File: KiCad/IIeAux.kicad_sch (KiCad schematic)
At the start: 15 parts, among them J1 Aux Slot, U1 SN74LVC245AN, U2 TangNano9K, U3 74LS245, U4 74LS374, U5 SN74LVC245AN, U6 SN74LVC245AN

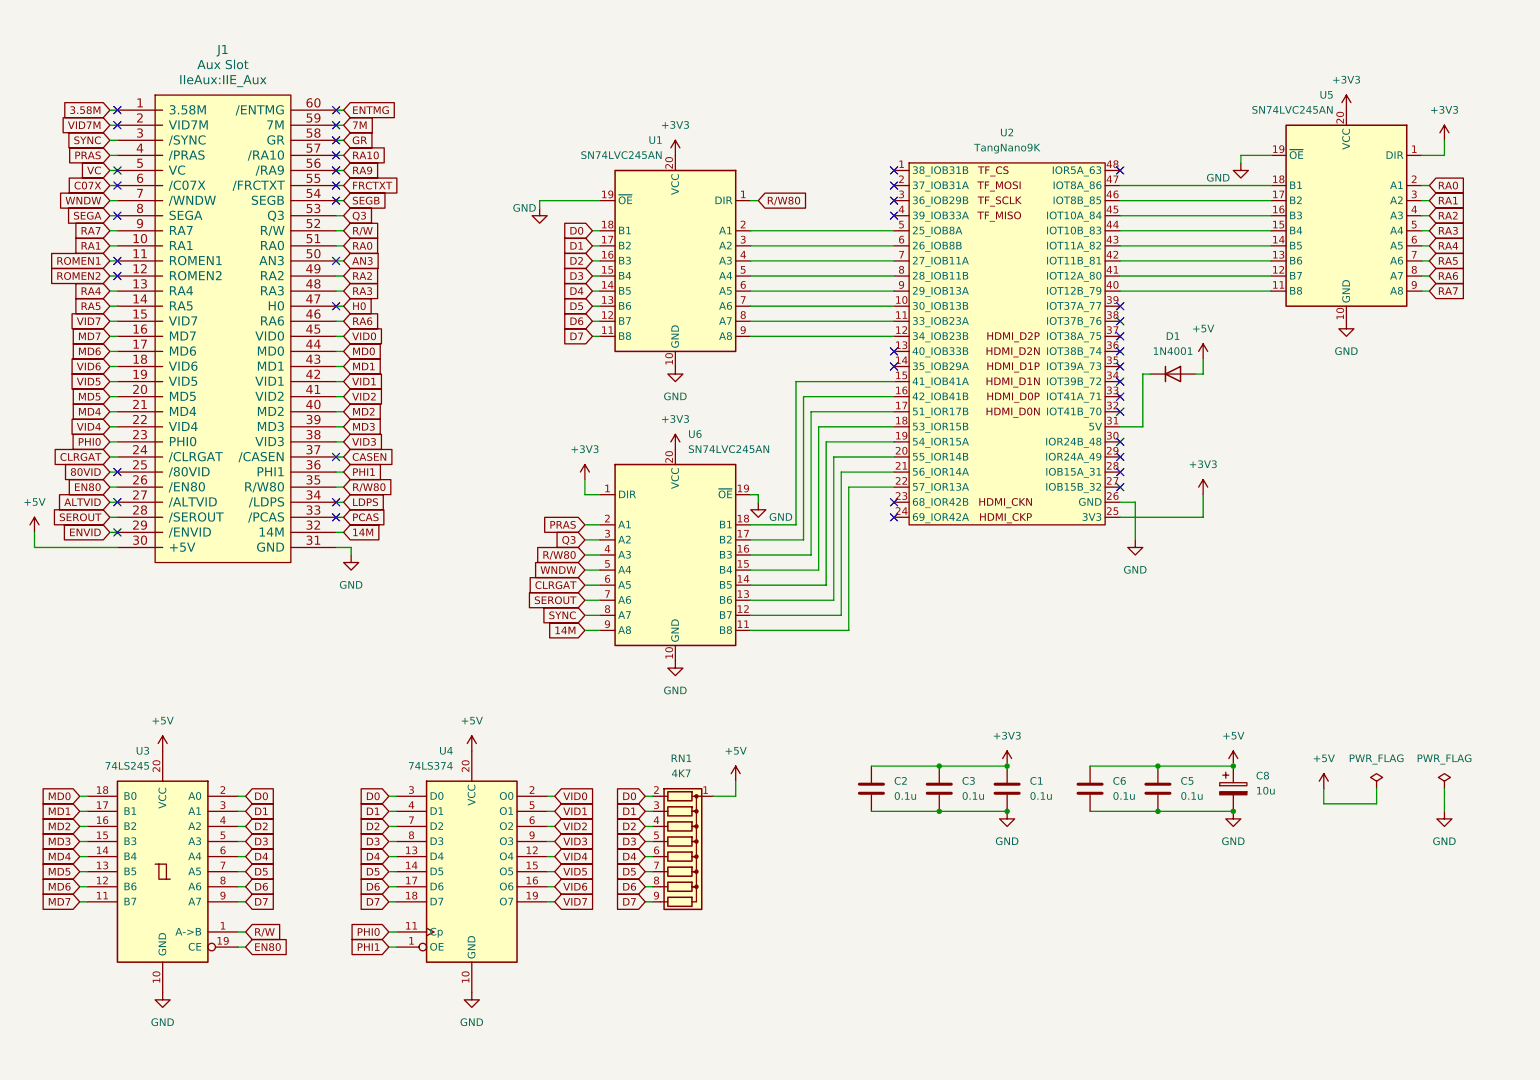
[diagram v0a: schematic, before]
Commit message: extended 64K RAM
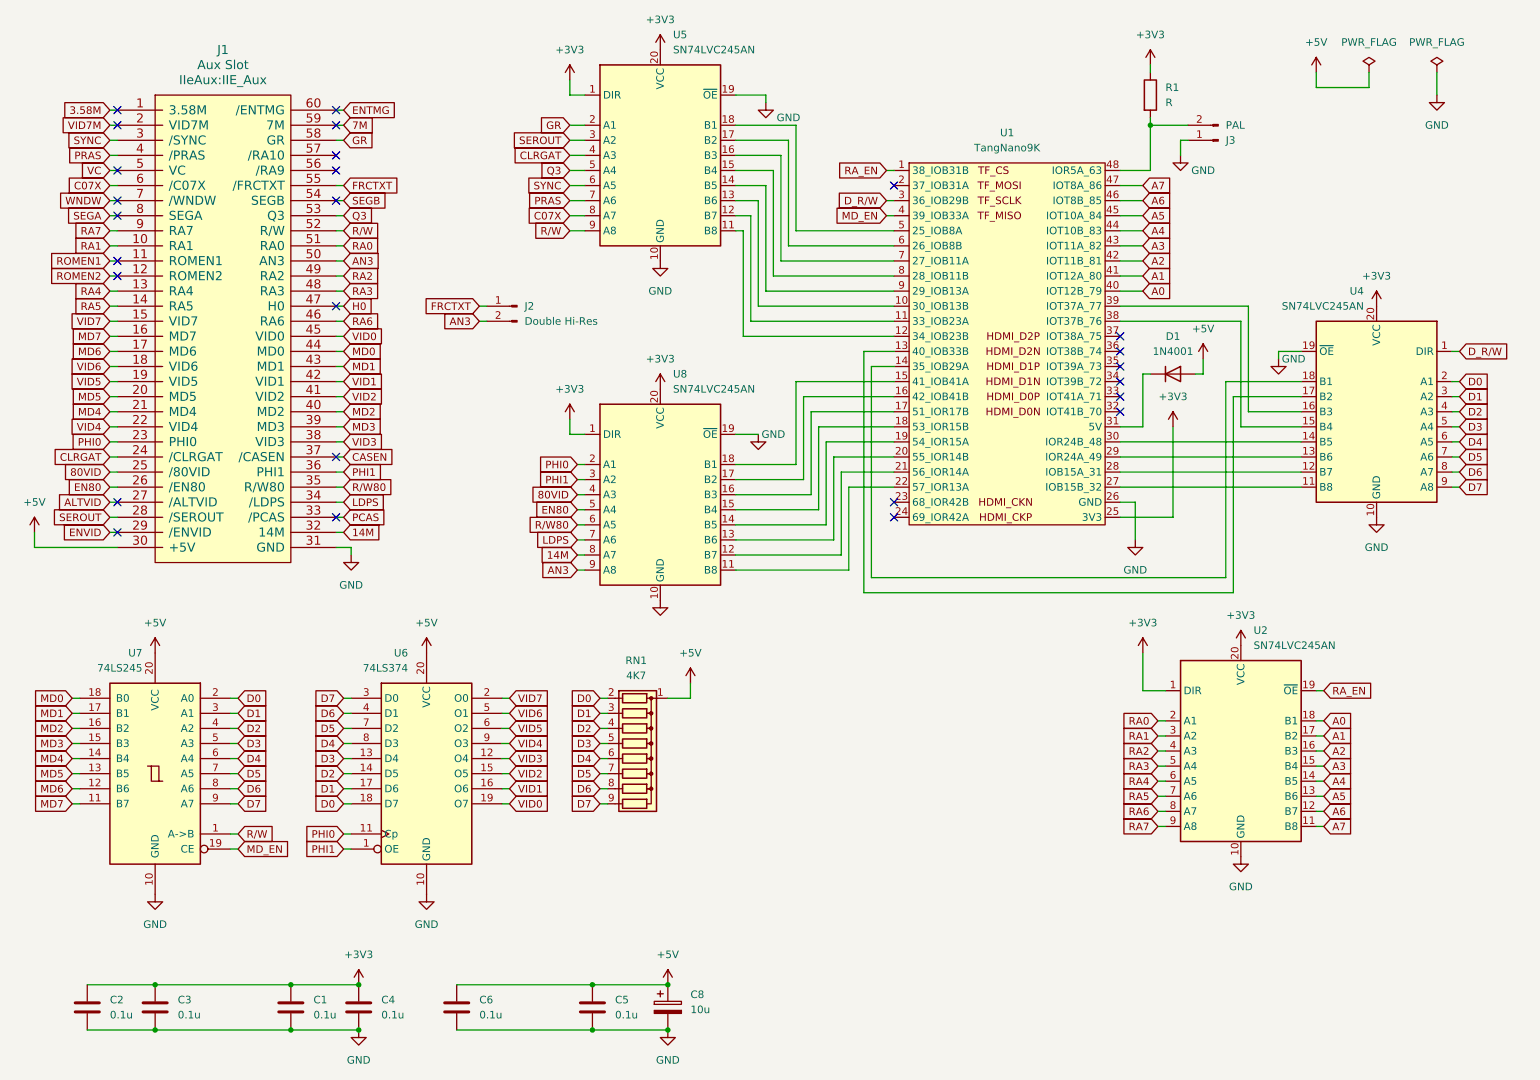
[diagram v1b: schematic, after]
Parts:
- added C4: 0.1u, IIeAux:C_Disc_D4.3mm_W1.9mm_P5.08mm, symbol IIeAux:C
- added J2: Double Hi-Res, IIeAux:PinHeader_1x02_P2.54mm_Horizontal, symbol IIeAux:Conn_01x02_Pin
- added J3: PAL, IIeAux:PinHeader_1x02_P2.54mm_Horizontal, symbol IIeAux:Conn_01x02_Pin
- added R1: R, IIeAux:R_Axial_DIN0207_L6.3mm_D2.5mm_P10.16mm_Horizontal, symbol Apple2_bus:R
- added U8: SN74LVC245AN, IIeAux:DIP-20_W7.62mm_Socket, symbol IIeAux:SN74LVC245AN
- renumbered U2 to U1, U5 to U2, U1 to U4, U6 to U5, U4 to U6, U3 to U7
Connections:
- net +3V3: now also C4.1, R1.1, U8.1 (DIR), U8.20 (VCC)
- net 14M: now also U8.8 (A7); no longer U5.9 (A8)
- net 80VID: now also U8.4 (A3)
- net AN3: now also J2.2 (Pin_2), U8.9 (A8)
- net C07X: now also U5.8 (A7)
- net CLRGAT: now also U5.4 (A3); no longer U5.6 (A5)
- net D0: now also U4.2 (A1), U6.18 (D7); no longer U4.18 (B1), U6.3 (D0)
- net D1: now also U4.3 (A2), U6.17 (D6); no longer U4.17 (B2), U6.4 (D1)
- net D2: now also U4.4 (A3), U6.14 (D5); no longer U4.16 (B3), U6.7 (D2)
- net D3: now also U4.5 (A4), U6.13 (D4); no longer U4.15 (B4), U6.8 (D3)
- net D4: now also U4.6 (A5), U6.8 (D3); no longer U4.14 (B5), U6.13 (D4)
- net D5: now also U4.7 (A6), U6.7 (D2); no longer U4.13 (B6), U6.14 (D5)
- net D6: now also U4.8 (A7), U6.4 (D1); no longer U4.12 (B7), U6.17 (D6)
- net D7: now also U4.9 (A8), U6.3 (D0); no longer U4.11 (B8), U6.18 (D7)
- net EN80: now also U8.5 (A4); no longer U7.19 (CE)
- net FRCTXT: now also J2.1 (Pin_1)
- net GND: now also C4.2, J3.1 (Pin_1), U8.10 (GND), U8.19 (~{OE}); no longer U2.19 (~{OE})
- net GR: now also U5.2 (A1)
- net LDPS: now also U8.7 (A6)
- net PHI0: now also U8.2 (A1)
- net PHI1: now also U8.3 (A2)
- net PRAS: now also U5.7 (A6); no longer U5.2 (A1)
- net Q3: now also U5.5 (A4); no longer U5.3 (A2)
- net R/W: now also U5.9 (A8)
- net R/W80: now also U8.6 (A5); no longer U4.1 (DIR), U5.4 (A3)
- net SEROUT: now also U5.3 (A2); no longer U5.7 (A6)
- net SYNC: now also U5.6 (A5); no longer U5.8 (A7)
- net VID0: now also U6.19 (O7); no longer U6.2 (O0)
- net VID1: now also U6.16 (O6); no longer U6.5 (O1)
- net VID2: now also U6.15 (O5); no longer U6.6 (O2)
- net VID3: now also U6.12 (O4); no longer U6.9 (O3)
- net VID4: now also U6.9 (O3); no longer U6.12 (O4)
- net VID5: now also U6.6 (O2); no longer U6.15 (O5)
- net VID6: now also U6.5 (O1); no longer U6.16 (O6)
- net VID7: now also U6.2 (O0); no longer U6.19 (O7)
- net WNDW: no longer U5.5 (A4)
- net A0: now reaches U1.40 (IOT12B_79)
- net A0: now also U2.18 (B1); no longer U2.11 (B8)
- net A1: now reaches U1.41 (IOT12A_80)
- net A1: now also U2.17 (B2); no longer U2.12 (B7)
- net A2: now reaches U1.42 (IOT11B_81)
- net A2: now also U2.16 (B3); no longer U2.13 (B6)
- net A3: now reaches U1.43 (IOT11A_82)
- net A3: now also U2.15 (B4); no longer U2.14 (B5)
- net A4: now reaches U1.44 (IOT10B_83)
- net A4: now also U2.14 (B5); no longer U2.15 (B4)
- net A5: now reaches U1.45 (IOT10A_84)
- net A5: now also U2.13 (B6); no longer U2.16 (B3)
- net A6: now reaches U1.46 (IOT8B_85)
- net A6: now also U2.12 (B7); no longer U2.17 (B2)
- net A7: now reaches U1.47 (IOT8A_86)
- net A7: now also U2.11 (B8); no longer U2.18 (B1)
- net at U1.5 (25_IOB8A): now also U5.18 (B1); no longer U4.2 (A1)
- net at U1.6 (26_IOB8B): now also U5.17 (B2); no longer U4.3 (A2)
- net at U1.7 (27_IOB11A): now also U5.16 (B3); no longer U4.4 (A3)
- net at U1.8 (28_IOB11B): now also U5.15 (B4); no longer U4.5 (A4)
- net at U1.9 (29_IOB13A): now also U5.14 (B5); no longer U4.6 (A5)
- net at U1.10 (30_IOB13B): now also U5.13 (B6); no longer U4.7 (A6)
- net at U1.11 (33_IOB23A): now also U5.12 (B7); no longer U4.8 (A7)
- net at U1.12 (34_IOB23B): now also U5.11 (B8); no longer U4.9 (A8)
- net at U1.22 (57_IOR13A): now also U8.11 (B8); no longer U5.11 (B8)
- net at U1.21 (56_IOR14A): now also U8.12 (B7); no longer U5.12 (B7)
- net at U1.20 (55_IOR14B): now also U8.13 (B6); no longer U5.13 (B6)
- net at U1.19 (54_IOR15A): now also U8.14 (B5); no longer U5.14 (B5)
- net at U1.18 (53_IOR15B): now also U8.15 (B4); no longer U5.15 (B4)
- net at U1.17 (51_IOR17B): now also U8.16 (B3); no longer U5.16 (B3)
- net at U1.16 (42_IOB41B): now also U8.17 (B2); no longer U5.17 (B2)
- net at U1.15 (41_IOB41A): now also U8.18 (B1); no longer U5.18 (B1)
- net RA_EN: now reaches U1.1 (38_IOB31B)
- net RA_EN: now also U2.19 (~{OE})
- net at U1.13 (40_IOB33B): now also U4.17 (B2)
- net at U1.14 (35_IOB29A): now also U4.18 (B1)
- net at U1.27 (IOB15B_32): now also U4.11 (B8)
- net at U1.28 (IOB15A_31): now also U4.12 (B7)
- net at U1.29 (IOR24A_49): now also U4.13 (B6)
- net D_R/W: now reaches U1.3 (36_IOB29B)
- net D_R/W: now also U4.1 (DIR)
- net at U1.30 (IOR24B_48): now also U4.14 (B5)
- net at U1.38 (IOT37B_76): now also U4.15 (B4)
- net at U1.39 (IOT37A_77): now also U4.16 (B3)
- net MD_EN: now reaches U1.4 (39_IOB33A)
- net MD_EN: now also U7.19 (CE)
- net at U1.48 (IOR5A_63): now also J3.2 (Pin_2), R1.2
- net RA10: no longer names the net of J1.57 (/RA10)
- net RA9: no longer names the net of J1.56 (/RA9)
- no-connect marks 43 -> 26
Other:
- moved on the sheet: C1, C2, C3, C5, C6, C8, RN1, U2, U4, U5, U6, U7

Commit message: correct data bus timing
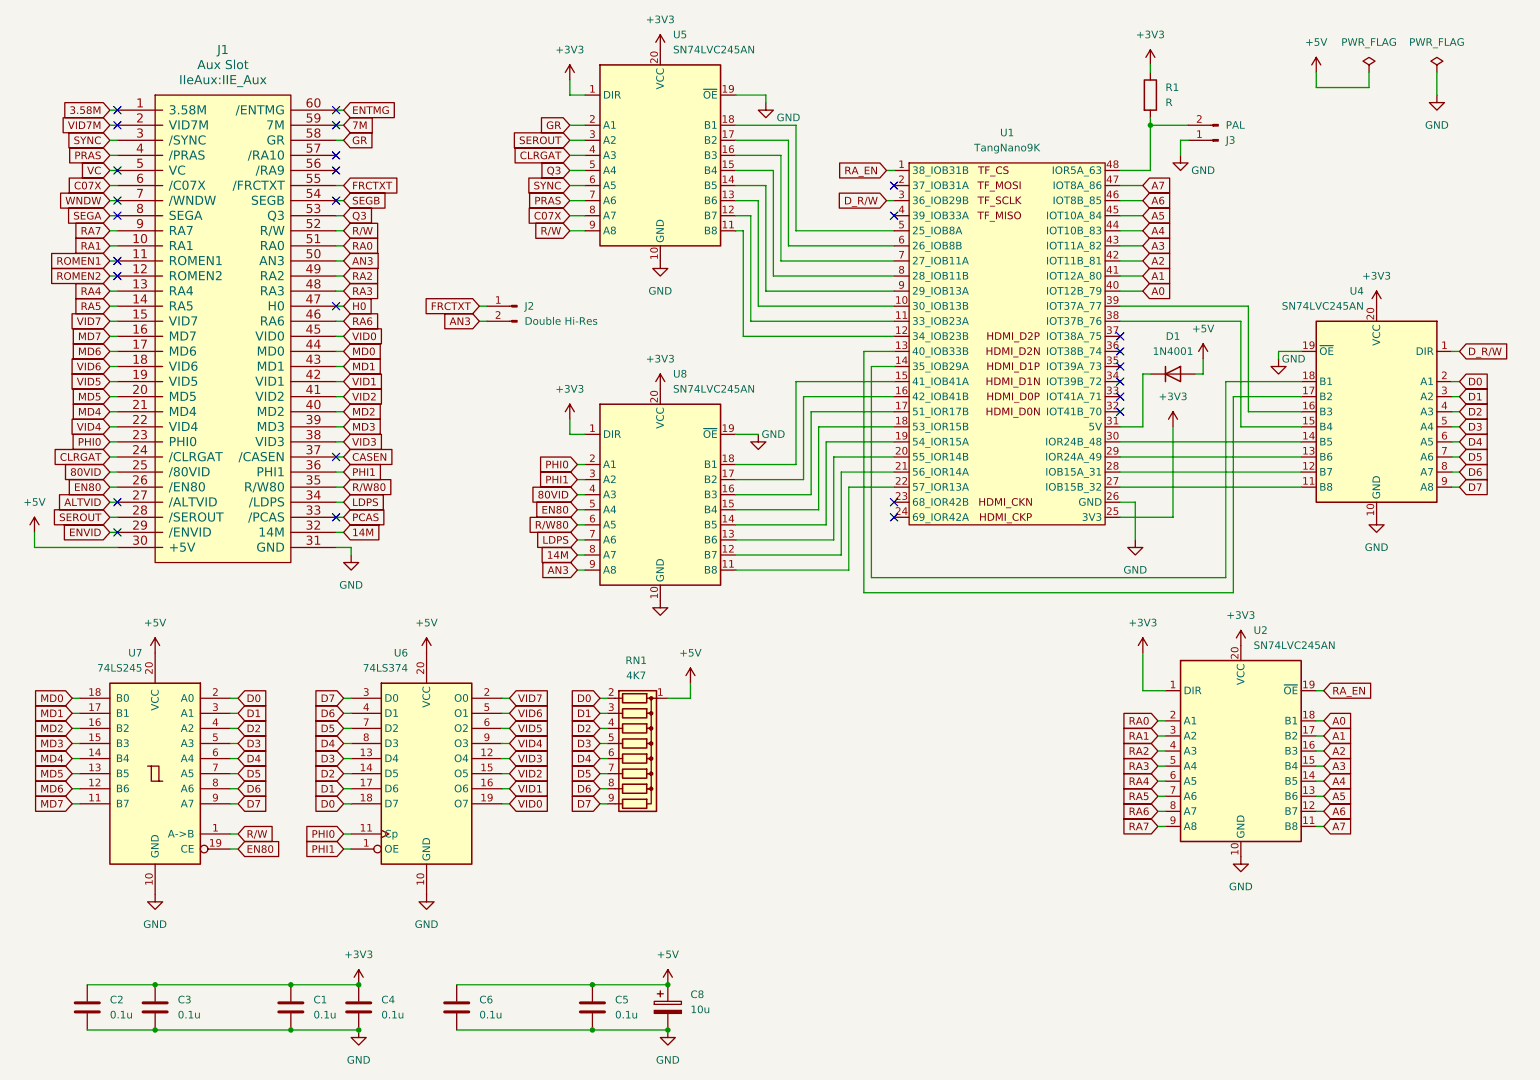
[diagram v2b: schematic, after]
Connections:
- net EN80: now also U7.19 (CE)
- net MD_EN: no longer names the net of U1.4 (39_IOB33A)
- net MD_EN: no longer U7.19 (CE)
- no-connect marks 26 -> 27
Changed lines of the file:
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@@
 	(title_block
 		(title "IIeAux")
-		(date "2026-03-28")
-		(rev "1.1.1")
+		(date "2026-04-26")
+		(rev "1.1.6")
 		(company "nanja.info")
 		(comment 1 "Apple IIe Aux Slot FPGA Card")
 		(comment 2 "Use SEROUT")
+		(comment 3 "correct data bus timing")
 	)
 	(junction
@@
 	)
 	(no_connect
+		(at 172.72 49.53)
+	)
+	(no_connect
 		(at 210.82 80.01)
 	)
@@
 	(wire
 		(pts
-			(xy 171.45 49.53) (xy 172.72 49.53)
-		)
-		(stroke
-			(width 0)
-			(type default)
-		)
-	)
-	(wire
-		(pts
 			(xy 119.38 109.22) (xy 120.65 109.22)
 		)
@@
 		)
 	)
-	(global_label "MD_EN"
-		(shape input)
-		(at 171.45 49.53 180)
-		(fields_autoplaced yes)
-		(effects
-			(font
-				(size 1.27 1.27)
-			)
-			(justify right)
-		)
-		(property "Intersheetrefs" "${INTERSHEET_REFS}"
-			(at 162.2963 49.53 0)
-			(effects
-				(font
-					(size 1.27 1.27)
-				)
-				(justify right)
-				(hide yes)
-			)
-		)
-	)
 	(global_label "SYNC"
 		(shape input)
@@
 		)
 	)
-	(global_label "MD_EN"
+	(global_label "EN80"
 		(shape input)
 		(at 62.23 156.21 0)
@@
 		)
 		(property "Intersheetrefs" "${INTERSHEET_REFS}"
-			(at 71.3837 156.21 0)
+			(at 70.1137 156.21 0)
 			(effects
 				(font

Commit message: PCB V2.0
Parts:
- removed R1: R, IIeAux:R_Axial_DIN0207_L6.3mm_D2.5mm_P10.16mm_Horizontal, symbol Apple2_bus:R
- added C7: 0.1u, IIeAux:C_Disc_D4.3mm_W1.9mm_P5.08mm, symbol IIeAux:C
- added R1, R2, R3: 10K, IIeAux:R_Axial_DIN0207_L6.3mm_D2.5mm_P10.16mm_Horizontal, symbol Apple2_bus:R_Small
- added SW1: SW2, IIeAux:SW_DIP_SPSTx02_Slide_9.78x7.26mm_W7.62mm_P2.54mm, symbol Switch:SW_DIP_x02
- added U4: 74LS245, IIeAux:DIP-20_W7.62mm_Socket, symbol IIeAux:74LS245
- J3: value PAL -> Mode
- renumbered U4 to U3
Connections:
- net +3V3: now also R1.1, R2.1, R3.1
- net +5V: now also C7.1, U4.20 (VCC)
- net 14M: now also U8.6 (A5); no longer U8.8 (A7)
- net 80VID: now also U8.3 (A2); no longer U8.4 (A3)
- net AN3: now also U5.7 (A6); no longer U8.9 (A8)
- net C07X: now also U4.19 (CE)
- net CLRGAT: no longer U5.4 (A3)
- net D0: now also U3.9 (A8), U4.2 (A0); no longer U3.2 (A1)
- net D1: now also U3.8 (A7), U4.3 (A1); no longer U3.3 (A2)
- net D2: now also U3.7 (A6), U4.4 (A2); no longer U3.4 (A3)
- net D3: now also U3.6 (A5), U4.5 (A3); no longer U3.5 (A4)
- net D4: now also U3.5 (A4), U4.6 (A4); no longer U3.6 (A5)
- net D5: now also U3.4 (A3), U4.7 (A5); no longer U3.7 (A6)
- net D6: now also U3.3 (A2), U4.8 (A6); no longer U3.8 (A7)
- net D7: now also U3.2 (A1), U4.9 (A7); no longer U3.9 (A8)
- net EN80: now also U8.4 (A3); no longer U8.5 (A4)
- net GND: now also J3.2 (Pin_2), U2.19 (~{OE}), C7.2, SW1.3, SW1.4, U4.1 (A->B), U4.10 (GND); no longer J3.1 (Pin_1)
- net GR: now also U5.3 (A2); no longer U5.2 (A1)
- net LDPS: no longer U8.7 (A6)
- net MD0: now also U4.18 (B0)
- net MD1: now also U4.17 (B1)
- net MD2: now also U4.16 (B2)
- net MD3: now also U4.15 (B3)
- net MD4: now also U4.14 (B4)
- net MD5: now also U4.13 (B5)
- net MD6: now also U4.12 (B6)
- net MD7: now also U4.11 (B7)
- net PHI1: no longer U8.3 (A2)
- net PRAS: now also U5.6 (A5); no longer U5.7 (A6)
- net Q3: now also U5.4 (A3); no longer U5.5 (A4)
- net R/W80: now also U8.5 (A4); no longer U8.6 (A5)
- net SEROUT: now also U8.7 (A6); no longer U5.3 (A2)
- net SYNC: now also U5.5 (A4); no longer U5.6 (A5)
- net D_RW: now reaches U1.48 (IOR5A_63)
- net D_RW: now also U3.1 (DIR); no longer J3.2 (Pin_2)
- net at U3.11 (B8): now also U1.13 (40_IOB33B); no longer U1.27 (IOB15B_32)
- net at U3.12 (B7): now also U1.14 (35_IOB29A); no longer U1.28 (IOB15A_31)
- net at U3.13 (B6): now also U1.27 (IOB15B_32); no longer U1.29 (IOR24A_49)
- net at U3.14 (B5): now also U1.28 (IOB15A_31); no longer U1.30 (IOR24B_48)
- net at U3.15 (B4): now also U1.29 (IOR24A_49); no longer U1.38 (IOT37B_76)
- net at U3.16 (B3): now also U1.30 (IOR24B_48); no longer U1.39 (IOT37A_77)
- net at U3.17 (B2): now also U1.38 (IOT37B_76); no longer U1.13 (40_IOB33B)
- net at U3.18 (B1): now also U1.39 (IOT37A_77); no longer U1.14 (35_IOB29A)
- net A0: no longer names the net of U1.40 (IOT12B_79)
- net A0: now also U2.11 (B8); no longer U2.18 (B1)
- net A1: no longer names the net of U1.41 (IOT12A_80)
- net A1: now also U2.12 (B7); no longer U2.17 (B2)
- net A2: no longer names the net of U1.42 (IOT11B_81)
- net A2: now also U2.13 (B6); no longer U2.16 (B3)
- net A3: no longer names the net of U1.43 (IOT11A_82)
- net A3: now also U2.14 (B5); no longer U2.15 (B4)
- net A4: no longer names the net of U1.44 (IOT10B_83)
- net A4: now also U2.15 (B4); no longer U2.14 (B5)
- net A5: no longer names the net of U1.45 (IOT10A_84)
- net A5: now also U2.16 (B3); no longer U2.13 (B6)
- net A6: no longer names the net of U1.46 (IOT8B_85)
- net A6: now also U2.17 (B2); no longer U2.12 (B7)
- net A7: no longer names the net of U1.47 (IOT8A_86)
- net A7: now also U2.18 (B1); no longer U2.11 (B8)
- net D_R/W: no longer names the net of U1.3 (36_IOB29B)
- net D_R/W: no longer U3.1 (DIR)
- net RA_EN: no longer names the net of U1.1 (38_IOB31B)
- net RA_EN: no longer U2.19 (~{OE})
- new net: R2.2, SW1.1, U8.8 (A7)
- new net: R3.2, SW1.2, U8.9 (A8)
- new net: J3.1 (Pin_1), R1.2, U5.2 (A1)
- no-connect marks 27 -> 31
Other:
- moved on the sheet: C2, C6, D1, RN1, U2, U3, U6, U7, U8
